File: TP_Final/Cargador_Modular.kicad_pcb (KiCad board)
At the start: 2 copper layers, 179 parts, among them J101 BG 1x2, J102 BD 1x2, J103 BG 1x2, J104 BG 1x3, J105 Poste 1x4, J106 Poste 2x4, J107 Poste 2x3, J108 BG2, J109 BG 1x3, J110 BG2, J111 Conector pol. 1x3, J112 BG2, J113 Conector pol. 1x3, J114 Conector pol. 1x3, J115 BG2, J116 BG2, K101 EC2-3NU, K102 EC2-3NU, K103 EC2-3NU, K104 EC2-3NU, Q101 2N3904, Q102 2N3904, Q103 2N3904, Q104 2N3904, Q105 2N3904, Q106 2N3904, Q107 2N3904, Q108 2N3904, Q109 2N3904, Q110 2N3904, SW101 SW_Push, SW102 KSR, SW103 KSR, SW104 KSR, SW105 KSR, U101 LM35-ZD, U102 STM32F103RBTx, U103 24LC256, U104 OP07, U105 OP07, U106 OP07, U107 LM7805_TO220, U108 LD3985M33R_TSOT23, Y101 8Mhz, Y102 32.768Khz

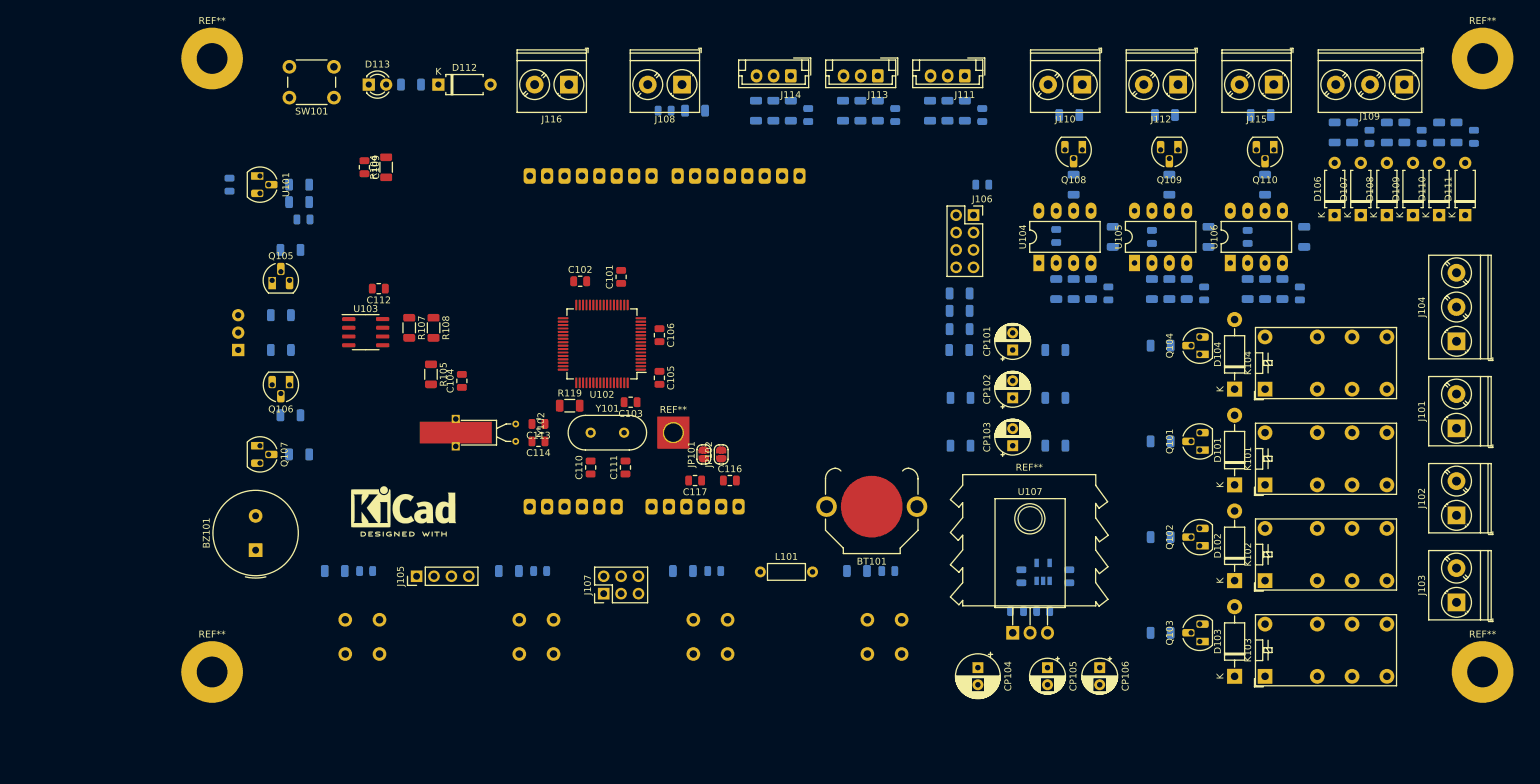
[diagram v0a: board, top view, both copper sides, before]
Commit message: Se avanza con el ruteo del PCB
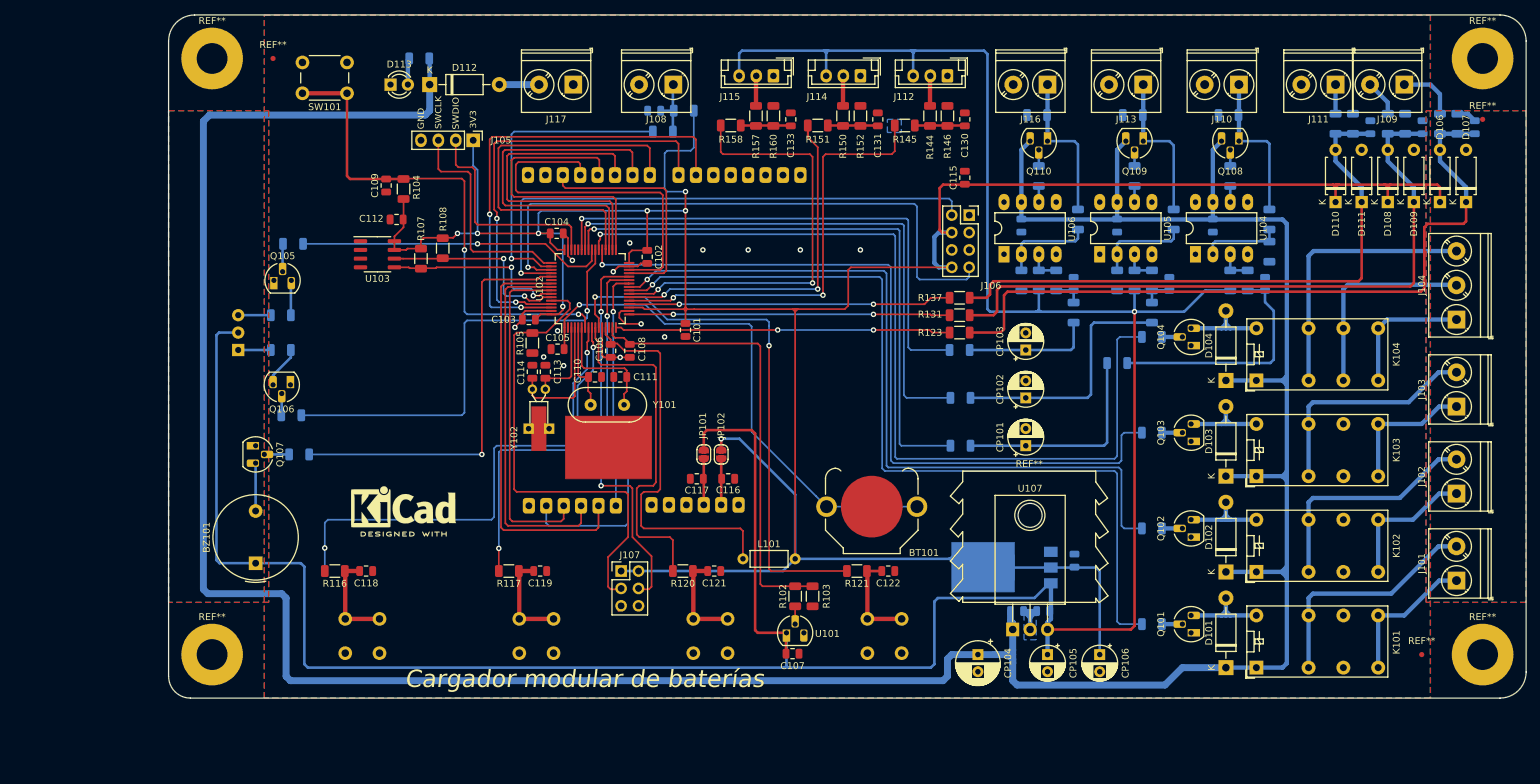
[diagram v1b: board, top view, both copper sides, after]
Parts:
- removed C138: .1, Capacitor_SMD:C_0805_2012Metric
- removed the J113 at (159.4, 44.5)
- removed the REF** at (129.5, 96.5)
- added J111: BG2, TerminalBlock_Phoenix:TerminalBlock_Phoenix_PT-1,5-2-5.0-H_1x02_P5.00mm_Horizontal, F.Cu at (226.2, 45.7)
- added J115: Conector pol. 1x3, Connector_JST:JST_EH_B3B-EH-A_1x03_P2.50mm_Vertical, F.Cu at (144.1, 44.5)
- added REF**: Fiducial_0.75mm_Mask1.5mm, Fiducial:Fiducial_0.75mm_Mask1.5mm, F.Cu at (238.8, 128.9)
- added REF**: Fiducial_0.75mm_Mask1.5mm, Fiducial:Fiducial_0.75mm_Mask1.5mm, F.Cu at (247.7, 50.8)
- added REF**: Fiducial_0.75mm_Mask1.5mm, Fiducial:Fiducial_0.75mm_Mask1.5mm, F.Cu at (71.1, 41.9)
- C107, C108, C115, C118, C119, C121, C122, C130, C131, C133, R102, R103, R116, R117, R120, R121, R123, R131, R137, R144, R145, R146, R150, R151, R152, R157, R158, R160: moved to F.Cu
- D112: footprint Diode_THT:D_A-405_P7.62mm_Horizontal -> Diode_THT:D_DO-41_SOD81_P10.16mm_Horizontal
- J102: value BD 1x2 -> BG 1x2
- J105: value Poste 1x4 -> Pin Header1x4
- J106: value Poste 2x4 -> Pin socket 2x4
- J107: value Poste 2x3 -> Pin Header 2x3
- J109: value BG 1x3 -> BG2; footprint TerminalBlock_Phoenix:TerminalBlock_Phoenix_PT-1,5-3-5.0-H_1x03_P5.00mm_Horizontal -> TerminalBlock_Phoenix:TerminalBlock_Phoenix_PT-1,5-2-5.0-H_1x02_P5.00mm_Horizontal
- K101, K102, K103, K104: value EC2-3NU -> 2FORM-C 2A 12VCC
- R119: moved to B.Cu
- SW102, SW103, SW104, SW105: value KSR -> KS01-B
- U108: value LD3985M33R_TSOT23 -> LD1117S33TR_SOT223; footprint Package_TO_SOT_SMD:TSOT-23-5 -> Package_TO_SOT_SMD:SOT-223-3_TabPin2
- Y102: footprint Crystal:Crystal_AT310_D3.0mm_L10.0mm_Horizontal_1EP_style2 -> Crystal:Crystal_C26-LF_D2.1mm_L6.5mm_Horizontal_1EP_style2
- moved C107 106.9 mm to (146.9, 128.8), turned to 0 degrees
- moved U101 101.7 mm to (146.1, 125.7), turned to 0 degrees
- moved R103 94.5 mm to (149.9, 120.4), turned to 270 degrees
- moved R102 94.1 mm to (147.3, 120.4), turned to 270 degrees
- moved J105 64.2 mm to (100.3, 53.8), turned to 270 degrees
- moved C108 51.3 mm to (123.2, 84.6), turned to 270 degrees
- moved R119 42.2 mm to (128.0, 52.6), turned to 180 degrees
- moved R161 33.1 mm to (188.6, 65.4)
- moved C132 33.1 mm to (180.3, 66.3)
- moved C134 33.0 mm to (188.0, 74.8)
- moved R153 33.0 mm to (182.9, 74.3)
- moved R156 33.0 mm to (185.4, 74.3)
- moved R159 33.0 mm to (182.9, 59.1), turned to 90 degrees
- moved R162 33.0 mm to (180.3, 74.3)
- moved Q110 33.0 mm to (184.2, 54.0)
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- renumbered J111 to J112, J112 to J113, J115 to J116, J116 to J117, R112 to R111, R111 to R112
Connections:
- J106 pad 1: /Control/UART_RX -> GNDA
- J106 pad 2: GNDA -> /Control/UART_RX
- J106 pad 3: +3V3 -> Net-(J106-Pad3)
- J106 pad 4: Net-(J106-Pad4) -> +3V3
- J106 pad 7: +3V3 -> /Control/UART_TX
- J106 pad 8: /Control/UART_TX -> +3V3
- R112 pad 2: /Control/LED_VERDE -> /Control/LED_ROJO
- R114 pad 2: /Control/LED_ROJO -> /Control/LED_VERDE
- R122 pad 2: Net-(J109-Pad3) -> Net-(J109-Pad1)
- R136 pad 2: Net-(J109-Pad1) -> Net-(J111-Pad1)
- R150 pad 2: Net-(J113-Pad2) -> Net-(J114-Pad2)
- R157 pad 2: Net-(J114-Pad2) -> Net-(J115-Pad2)
- SW102 pad 2: GNDA -> Net-(C118-Pad1)
- SW102 pad 3: (no net) -> GNDA
- SW102 pad 4: (no net) -> GNDA
- SW103 pad 2: GNDA -> Net-(C119-Pad1)
- SW103 pad 3: (no net) -> GNDA
- SW103 pad 4: (no net) -> GNDA
- SW104 pad 2: GNDA -> Net-(C121-Pad1)
- SW104 pad 3: (no net) -> GNDA
- SW104 pad 4: (no net) -> GNDA
- SW105 pad 2: GNDA -> Net-(C122-Pad1)
- SW105 pad 3: (no net) -> GNDA
- SW105 pad 4: (no net) -> GNDA
- U102 pad 55: /Control/LCD_RS -> /Control/LCD_RW
- U102 pad 56: /Control/LCD_RW -> /Control/LCD_RS
- U102 pad 8: /Control/KEYBOARD_ESC -> /Control/KEYBOARD_ENT
- U102 pad 9: /Control/KEYBOARD_ENT -> /Control/KEYBOARD_ESC
- U108 pad 1: +5V -> GNDA
- U108 pad 2: GNDA -> +3V3
- Y102 pad 1: Net-(C113-Pad2) -> Net-(C114-Pad2)
- Y102 pad 2: Net-(C114-Pad2) -> Net-(C113-Pad2)
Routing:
- net +12V: track 0.00 -> 468.4 mm
- net +3V3: track 0.00 -> 443.9 mm, vias 0 -> 8
- net +5V: track 0.00 -> 436.2 mm, vias 0 -> 1
- net Net-(R110-Pad2): track 0.00 -> 131.2 mm, vias 0 -> 1
- net Net-(R101-Pad2): track 0.00 -> 125.4 mm, vias 0 -> 1
- net Net-(R109-Pad2): track 0.00 -> 113.5 mm, vias 0 -> 1
- net Net-(R106-Pad2): track 0.00 -> 112.6 mm, vias 0 -> 1
- net Net-(C124-Pad1): track 0.00 -> 106.7 mm
- net Net-(C126-Pad1): track 0.00 -> 97.1 mm
- net /Control/UART_TX: track 0.00 -> 89.1 mm, vias 0 -> 1
- net /Control/PWM_1: track 0.00 -> 87.2 mm, vias 0 -> 1
- net Net-(C127-Pad1): track 0.00 -> 87.0 mm
- net /Control/PWM_2: track 0.00 -> 81.9 mm, vias 0 -> 1
- net /Control/UART_RX: track 0.00 -> 80.1 mm, vias 0 -> 1
- net /Control/KEYBOARD_DOWN: track 0.00 -> 79.1 mm, vias 0 -> 2
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- added copper zone on B.Cu, net GNDA
- added copper zone on F.Cu, net GNDA
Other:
- board outline added: 198.1 x 99.7 mm
- net class prueba added: clearance 0.3048, trace_width 0.25, via_dia 0.8, via_drill 0.4
- board text added: "3V3"
- board text added: "Cargador modular de baterías"
- board text added: "GND"
- board text added: "SWCLK"
- board text added: "SWDIO"

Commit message: se avanza con el ruteo del PCB
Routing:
- net GNDA: vias 13 -> 15

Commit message: se corrigen errores detectados con DRC
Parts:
- removed the J111 at (226.2, 45.7)
- removed the REF** at (238.8, 128.9)
- removed the REF** at (247.7, 50.8)
- removed the REF** at (71.1, 41.9)
- removed the REF** at (62.2, 41.9)
- removed the REF** at (62.2, 128.9)
- removed the REF** at (247.7, 41.9)
- removed the REF** at (247.7, 128.9)
- removed the REF** at (181.5, 108.6)
- added FID101: Fiducial, Fiducial:Fiducial_0.75mm_Mask1.5mm, F.Cu at (71.1, 41.9)
- added FID102: Fiducial, Fiducial:Fiducial_0.75mm_Mask1.5mm, F.Cu at (247.7, 50.8)
- added FID103: Fiducial, Fiducial:Fiducial_0.75mm_Mask1.5mm, F.Cu at (238.8, 128.9)
- added H101: MountingHole, MountingHole:MountingHole_4.5mm_Pad, F.Cu at (62.9, 128.3)
- added H102: MountingHole, MountingHole:MountingHole_4.5mm_Pad, F.Cu at (62.9, 42.5)
- added H103: MountingHole, MountingHole:MountingHole_4.5mm_Pad, F.Cu at (247.0, 128.3)
- added H104: MountingHole, MountingHole:MountingHole_4.5mm_Pad, F.Cu at (247.0, 42.5)
- added HS101: Heatsink, Heatsink:Heatsink_Aavid-TV5G_TO220_Horizontal, F.Cu at (181.5, 108.6)
- J109: value BG2 -> 2 x BG2; footprint TerminalBlock_Phoenix:TerminalBlock_Phoenix_PT-1,5-2-5.0-H_1x02_P5.00mm_Horizontal -> TerminalBlock_Phoenix:TerminalBlock_Phoenix_PT-1,5-4-5.0-H_1x04_P5.00mm_Horizontal
- moved REF** 69.5 mm to (157.5, 90.2)
- moved C113 0.13 mm to (111.0, 87.6)
- moved C114 0.13 mm to (108.8, 87.6)
- renumbered J112 to J111, J113 to J112, J114 to J113, J115 to J114, J116 to J115, J117 to J116
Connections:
- R136 pad 2: Net-(J111-Pad1) -> Net-(J109-Pad3)
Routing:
- net Net-(J111-Pad1): track 4.27 -> 0.00 mm
- net Net-(J109-Pad3): track 0.00 -> 4.27 mm
- net GNDA: track 41.4 -> 38.9 mm
- net +3V3: track 443.9 -> 442.3 mm
- net +12V: track 468.4 -> 467.3 mm
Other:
- board text added: "(-)PWM1(+)"
- board text added: "(-)PWM2(+)"
- board text added: "(-)PWM3(+)"
- board text added: "5V"
- board text added: "ALARMA"
- board text added: "B(+)"
- board text added: "B(-)"
- board text added: "BOOT0"
- board text added: "BOOT1"
- board text added: "C(+)"
- board text added: "C(-)"
- board text added: "Energía Garantizada"
- board text added: "Fuente 1"
- board text added: "Fuente 2"
- board text added: "Fuente 3"
- board text added: "P. Emergencia"
- board text added: "RX"
- board text added: "Reset"
- board text added: "Sensor 1"
- board text added: "Sensor 2"
- board text added: "Sensor 3"
- board text added: "TX"
- board text added: "VCC GND"
- board text added: "com."
- board text added: "n.a."
- board text added: "n.c."
- board text added: "proba"

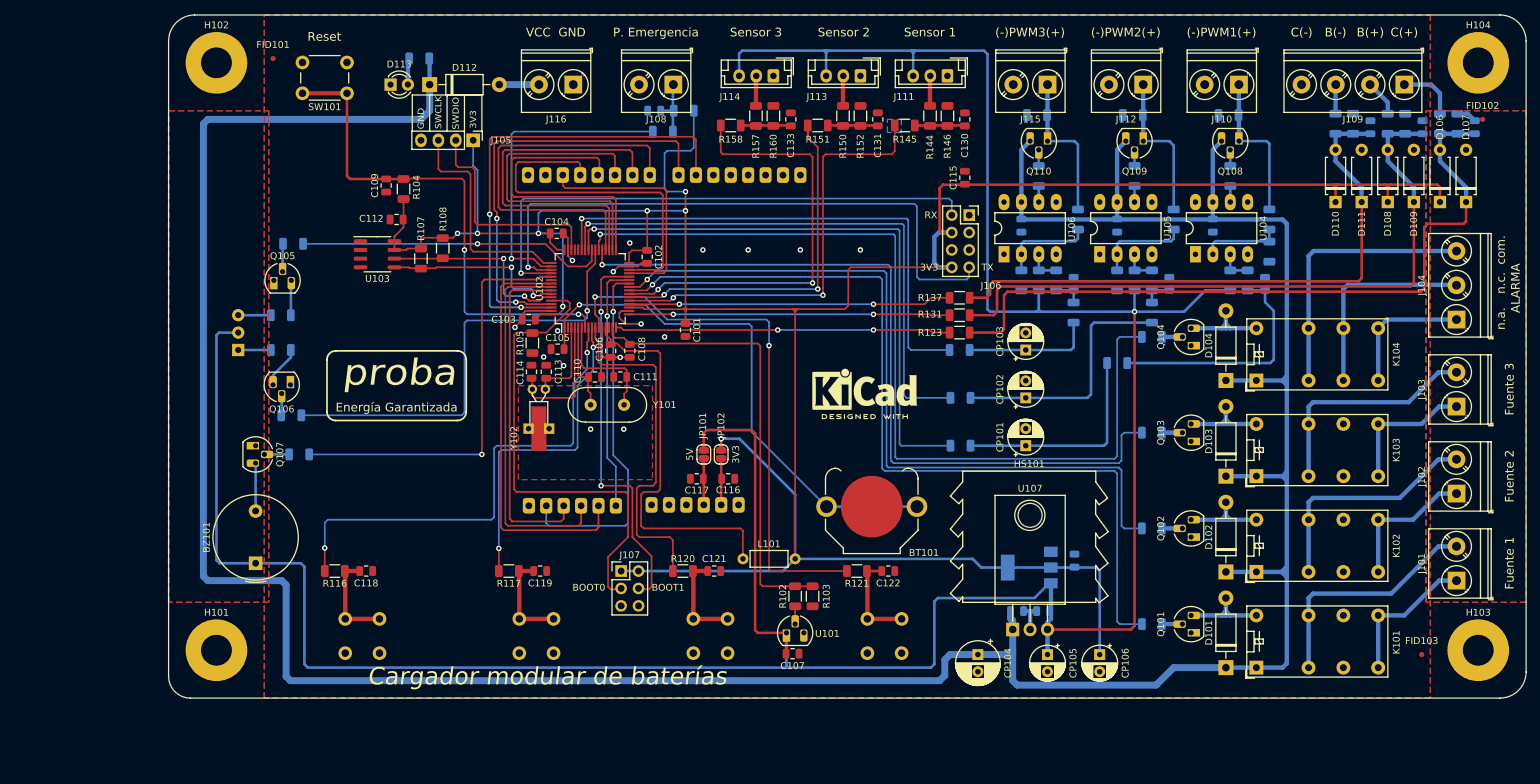
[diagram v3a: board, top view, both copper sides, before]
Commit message: Se cambio huella del portapilas y se completo el relleno de cobre
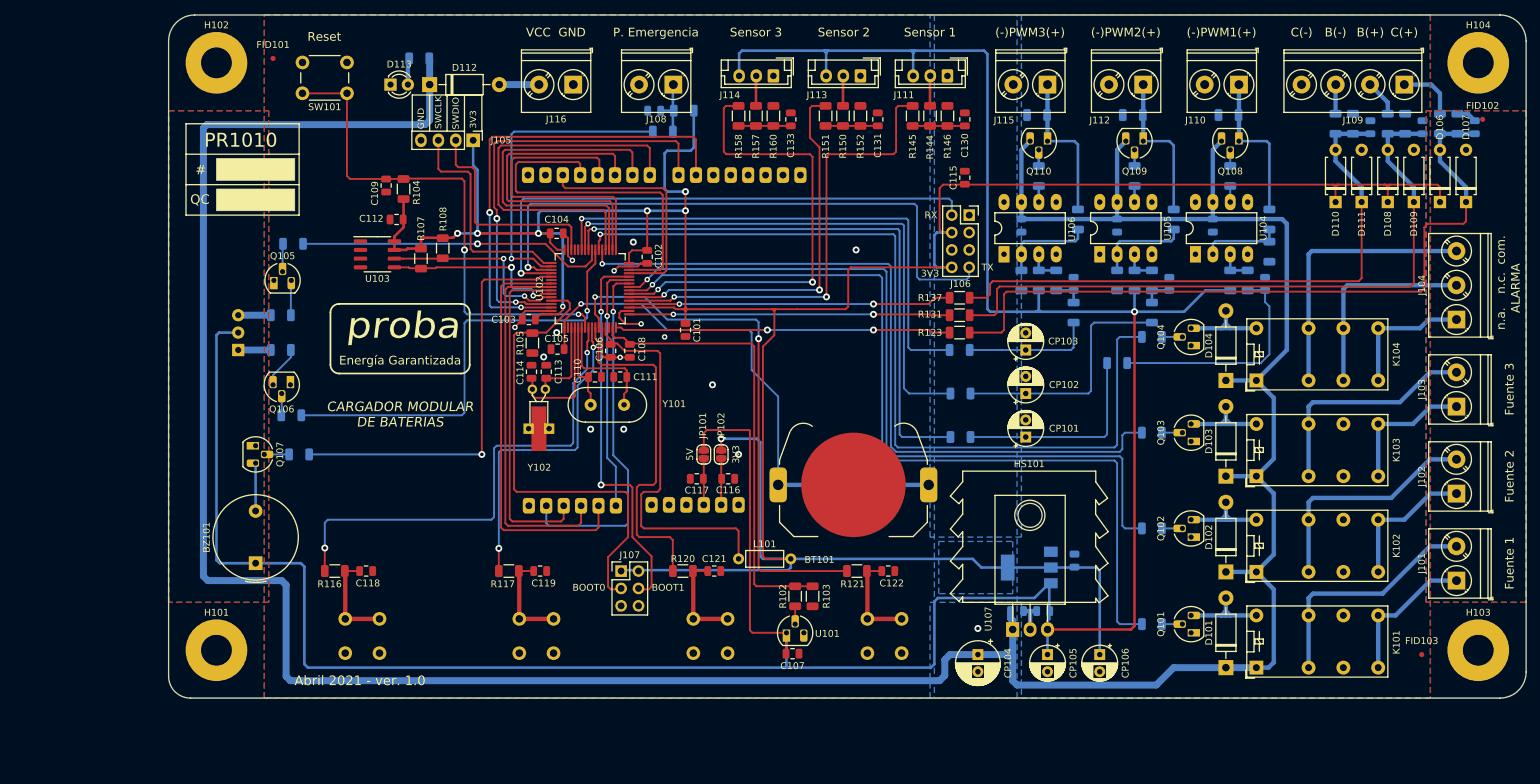
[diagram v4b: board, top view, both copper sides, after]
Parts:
- BT101: footprint Battery:BatteryHolder_Keystone_3001_1x12mm -> Battery:BatteryHolder_Keystone_3034_1x20mm
- REF**: moved to B.Cu
- moved REF** 69.2 mm to (89.4, 102.6)
- moved BT101 4.15 mm to (155.8, 104.1)
- moved R145 1.81 mm to (164.5, 50.3), turned to 270 degrees
- moved R158 1.81 mm to (139.1, 50.3), turned to 270 degrees
- moved R151 1.81 mm to (151.8, 50.3), turned to 270 degrees
- moved CP101 1.27 mm to (181.0, 97.2)
- moved R126 1.27 mm to (171.4, 97.2)
- moved CP102 0.63 mm to (181.0, 90.8)
- moved L101 0.63 mm to (139.1, 114.9)
- moved R140 0.63 mm to (171.4, 90.8)
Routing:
- net +12V: track 467.3 -> 453.9 mm
- net +3V3: track 442.3 -> 450.6 mm
- net /Control/ADC_5: track 63.4 -> 68.8 mm
- net /Control/ADC_6: track 53.3 -> 57.8 mm
- net /Control/ADC_7: track 63.4 -> 67.7 mm
- net Net-(R109-Pad2): track 113.5 -> 109.9 mm
- net Net-(R110-Pad2): track 131.2 -> 127.8 mm
- net Net-(BT101-Pad1): track 77.9 -> 79.9 mm
- net /Control/PWM_1: track 87.2 -> 85.8 mm
- net Net-(C125-Pad1): track 34.8 -> 33.4 mm
- net Net-(CP101-Pad1): track 31.7 -> 30.4 mm
- net /Control/PWM_2: track 81.9 -> 81.0 mm
- net Net-(C106-Pad1): track 57.5 -> 56.6 mm
- net Net-(D104-Pad2): track 13.9 -> 13.2 mm
- net Net-(CP102-Pad1): track 36.9 -> 36.3 mm
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- added copper zone on B.Cu, net +3V3
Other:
- net class prueba: trace_width 0.25 -> 0.2794
- board text added: "#"
- board text added: "Abril 2021 - ver. 1.0"
- board text added: "CARGADOR MODULAR DE BATERIAS"
- board text added: "PR1010"
- board text added: "QC"
- board text removed: "Cargador modular de baterías"

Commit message: se completa el relleno de cobre
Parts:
- REF**: moved to F.Cu
